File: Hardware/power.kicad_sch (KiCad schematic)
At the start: 71 parts, among them IC1 MIC5060YML-TR, J8 DeployLipo, J9 UCLipo, Q10 DMP3099L, Q11 SQS141ELNW-T1_GE3, Q12 SQS141ELNW-T1_GE3, Q5 BSZ025N04LS, Q8 DMP3099L, Q9 DMP3099L, U10 LTC4412xS6, U11 MP28167GQ-A-Z, U12 INA219AxDCN, U14 LTC4412xS6, U16 SC4215, U17 LTC4412xS6, U22 LTC4412xS6, U9 LTC4412xS6

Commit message: hardware updates
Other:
- note added: "0x45"
- note removed: "0x40"
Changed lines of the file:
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@@
 		)
 	)
-	(text "0x40"
+	(text "0x45\n"
 		(exclude_from_sim no)
 		(at 137.414 116.332 0)

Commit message: Ordering v3
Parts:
- IC1: footprint SON65P300X300X100-9N-D -> iclr:SON65P300X300X100-9N-D
- R25, R45: value 80k -> 75k
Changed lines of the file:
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@@
 			)
 		)
-		(property "Value" "80k"
+		(property "Value" "75k"
 			(at 118.11 31.7499 0)
 			(effects
@@
 			)
 		)
-		(property "Footprint" "SON65P300X300X100-9N-D"
+		(property "Footprint" "iclr:SON65P300X300X100-9N-D"
 			(at 123.19 265.1 0)
 			(effects
@@
 			)
 		)
-		(property "Value" "80k"
+		(property "Value" "75k"
 			(at 81.28 31.7499 0)
 			(effects

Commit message: Adding some 3d models
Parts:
- Q5: footprint iclr-hw:BSZ025N04LS -> iclr:BSZ025N04LS
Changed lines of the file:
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@@
 	(label "RBUS_24V_GATE"
 		(at 264.16 129.54 0)
-		(fields_autoplaced yes)
 		(effects
 			(font
@@
 	(label "Deploy_Lipo+"
 		(at 38.1 44.45 180)
-		(fields_autoplaced yes)
 		(effects
 			(font
@@
 	(label "Deploy_Lipo+"
 		(at 270.51 97.79 0)
-		(fields_autoplaced yes)
 		(effects
 			(font
@@
 	(label "BB_VCC"
 		(at 190.5 78.74 180)
-		(fields_autoplaced yes)
 		(effects
 			(font
@@
 	(label "DEP_IN"
 		(at 283.21 142.24 180)
-		(fields_autoplaced yes)
 		(effects
 			(font
@@
 	(label "BB_ALT"
 		(at 120.65 52.07 0)
-		(fields_autoplaced yes)
 		(effects
 			(font
@@
 	(label "BB_IN"
 		(at 78.74 25.4 0)
-		(fields_autoplaced yes)
 		(effects
 			(font
@@
 	(label "UC_Lipo+"
 		(at 30.48 115.57 180)
-		(fields_autoplaced yes)
 		(effects
 			(font
@@
 	(label "DEP_IN"
 		(at 95.25 120.65 90)
-		(fields_autoplaced yes)
 		(effects
 			(font
@@
 	(label "FBIn"
 		(at 247.65 31.75 180)
-		(fields_autoplaced yes)
 		(effects
 			(font
@@
 	(label "BB_SDA"
 		(at 97.79 83.82 180)
-		(fields_autoplaced yes)
 		(effects
 			(font
@@
 	(label "BB_SCL"
 		(at 97.79 78.74 180)
-		(fields_autoplaced yes)
 		(effects
 			(font
@@
 	(label "DEP_SWITCH_IN"
 		(at 95.25 129.54 270)
-		(fields_autoplaced yes)
 		(effects
 			(font
@@
 	(label "BB_OUT"
 		(at 170.18 93.98 180)
-		(fields_autoplaced yes)
 		(effects
 			(font
@@
 	(label "BB_FB"
 		(at 130.81 78.74 180)
-		(fields_autoplaced yes)
 		(effects
 			(font
@@
 	(label "DEP_IN"
 		(at 234.95 143.51 180)
-		(fields_autoplaced yes)
 		(effects
 			(font
@@
 	(label "BB_IN"
 		(at 76.2 67.31 180)
-		(fields_autoplaced yes)
 		(effects
 			(font
@@
 	(label "BB_OUT"
 		(at 223.52 71.12 180)
-		(fields_autoplaced yes)
 		(effects
 			(font
@@
 	(label "BB_VCC"
 		(at 142.24 52.07 180)
-		(fields_autoplaced yes)
 		(effects
 			(font
@@
 	(label "BB_IN"
 		(at 77.47 161.29 180)
-		(fields_autoplaced yes)
 		(effects
 			(font
@@
 	(label "BB_OUT"
 		(at 199.39 22.86 180)
-		(fields_autoplaced yes)
 		(effects
 			(font
@@
 	(label "BB_IN"
 		(at 76.2 115.57 180)
-		(fields_autoplaced yes)
 		(effects
 			(font
@@
 	(label "Deploy_Lipo+"
 		(at 245.11 100.33 180)
-		(fields_autoplaced yes)
 		(effects
 			(font
@@
 	(label "BB_FB"
 		(at 142.24 93.98 0)
-		(fields_autoplaced yes)
 		(effects
 			(font
@@
 	(label "BB_ALT"
 		(at 130.81 68.58 180)
-		(fields_autoplaced yes)
 		(effects
 			(font
@@
 	(label "BB_SDA"
 		(at 130.81 73.66 180)
-		(fields_autoplaced yes)
 		(effects
 			(font
@@
 	(label "DEP_IN"
 		(at 281.94 82.55 180)
-		(fields_autoplaced yes)
 		(effects
 			(font
@@
 	(label "DEP_IN"
 		(at 281.94 110.49 180)
-		(fields_autoplaced yes)
 		(effects
 			(font
@@
 	(label "Deploy_Lipo_Gate"
 		(at 270.51 102.87 0)
-		(fields_autoplaced yes)
 		(effects
 			(font
@@
 	(label "UC_Lipo+"
 		(at 53.34 44.45 0)
-		(fields_autoplaced yes)
 		(effects
 			(font
@@
 	(label "BB_IN"
 		(at 86.36 58.42 0)
-		(fields_autoplaced yes)
 		(effects
 			(font
@@
 	(label "BB_VCC"
 		(at 73.66 81.28 0)
-		(fields_autoplaced yes)
 		(effects
 			(font
@@
 	(label "BB_SCL"
 		(at 130.81 71.12 180)
-		(fields_autoplaced yes)
 		(effects
 			(font
@@
 	(label "Deploy_Lipo+"
 		(at 184.15 143.51 0)
-		(fields_autoplaced yes)
 		(effects
 			(font
@@
 	(label "RBUS_24V_GATE"
 		(at 270.51 74.93 0)
-		(fields_autoplaced yes)
 		(effects
 			(font
@@
 	(label "DEP_IN"
 		(at 115.57 25.4 0)
-		(fields_autoplaced yes)
 		(effects
 			(font
@@
 	(label "DEP_SWITCH_IN"
 		(at 92.71 152.4 180)
-		(fields_autoplaced yes)
 		(effects
 			(font
@@
 	(label "Deploy_Lipo_Gate"
 		(at 215.9 130.81 0)
-		(fields_autoplaced yes)
 		(effects
 			(font
@@
 		(shape input)
 		(at 91.44 172.72 180)
-		(fields_autoplaced yes)
 		(effects
 			(font
@@
 		(shape output)
 		(at 128.27 34.29 0)
-		(fields_autoplaced yes)
 		(effects
 			(font
@@
 		(shape input)
 		(at 140.97 119.38 0)
-		(fields_autoplaced yes)
 		(effects
 			(font
@@
 		(shape input)
 		(at 30.48 67.31 180)
-		(fields_autoplaced yes)
 		(effects
 			(font
@@
 		(shape input)
 		(at 250.19 142.24 180)
-		(fields_autoplaced yes)
 		(effects
 			(font
@@
 		(shape input)
 		(at 240.03 72.39 180)
-		(fields_autoplaced yes)
 		(effects
 			(font
@@
 		(shape output)
 		(at 175.26 118.11 0)
-		(fields_autoplaced yes)
 		(effects
 			(font
@@
 		(shape input)
 		(at 270.51 69.85 0)
-		(fields_autoplaced yes)
 		(effects
 			(font
@@
 		(shape input)
 		(at 140.97 121.92 0)
-		(fields_autoplaced yes)
 		(effects
 			(font
@@
 		(shape output)
 		(at 91.44 34.29 0)
-		(fields_autoplaced yes)
 		(effects
 			(font
@@
 			)
 		)
-		(property "Footprint" "iclr-hw:BSZ025N04LS"
+		(property "Footprint" "iclr:BSZ025N04LS"
 			(at 206.68 132.08 0)
 			(effects

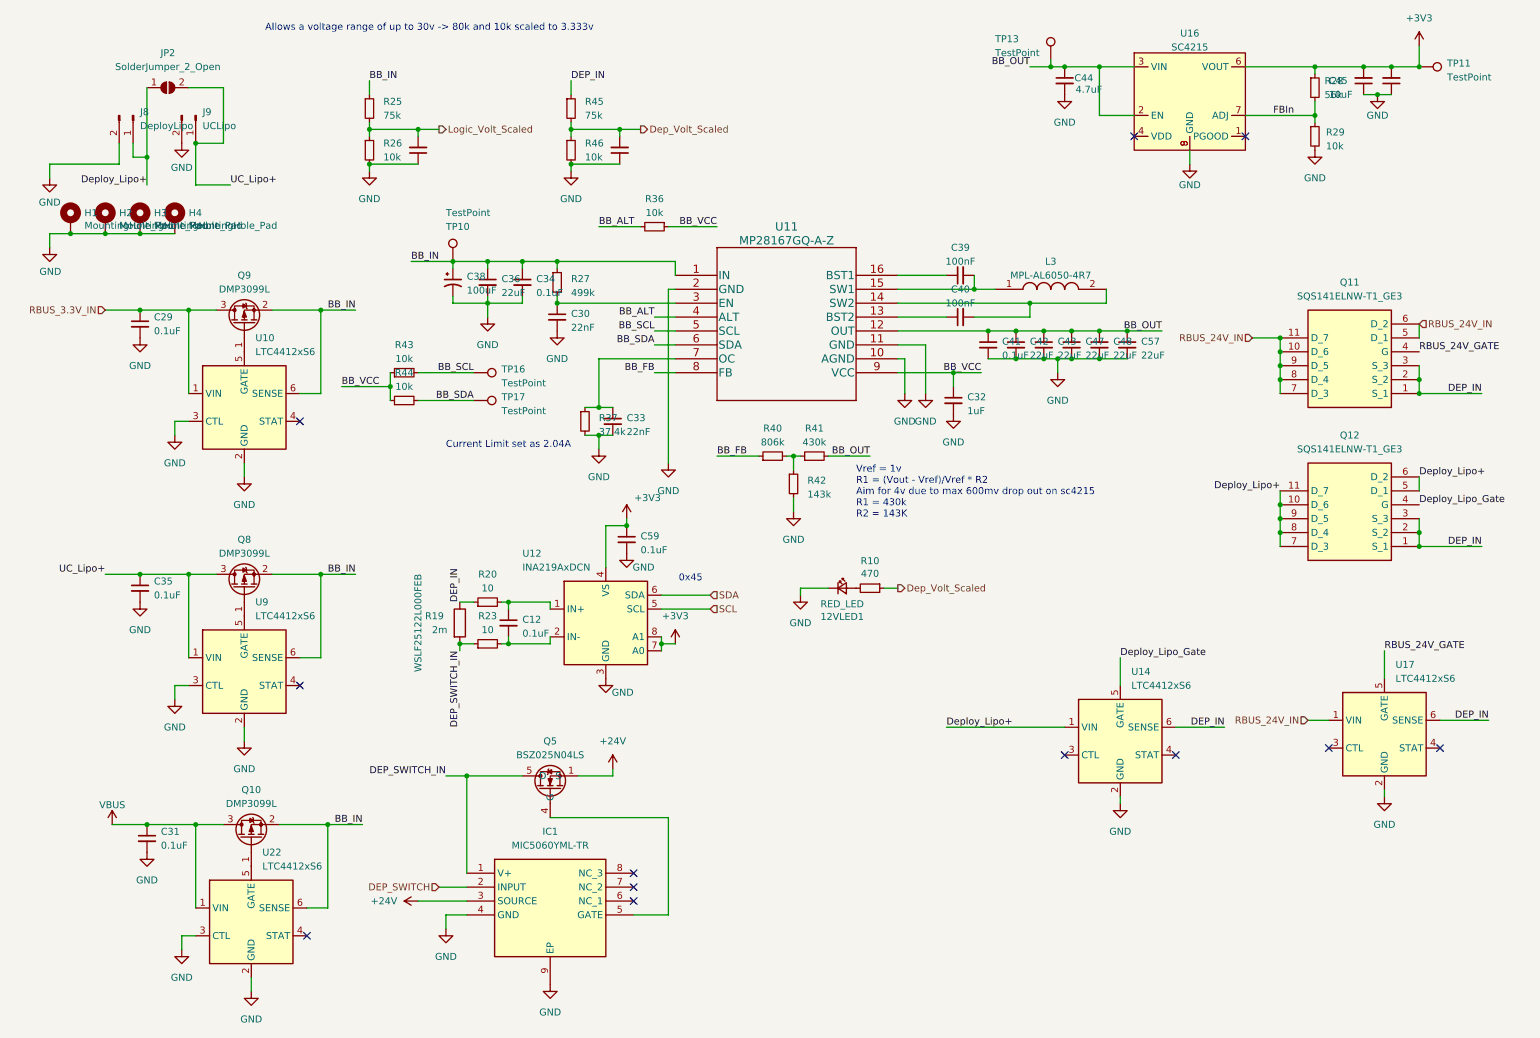
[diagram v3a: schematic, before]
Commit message: cleaned up schematic and bom
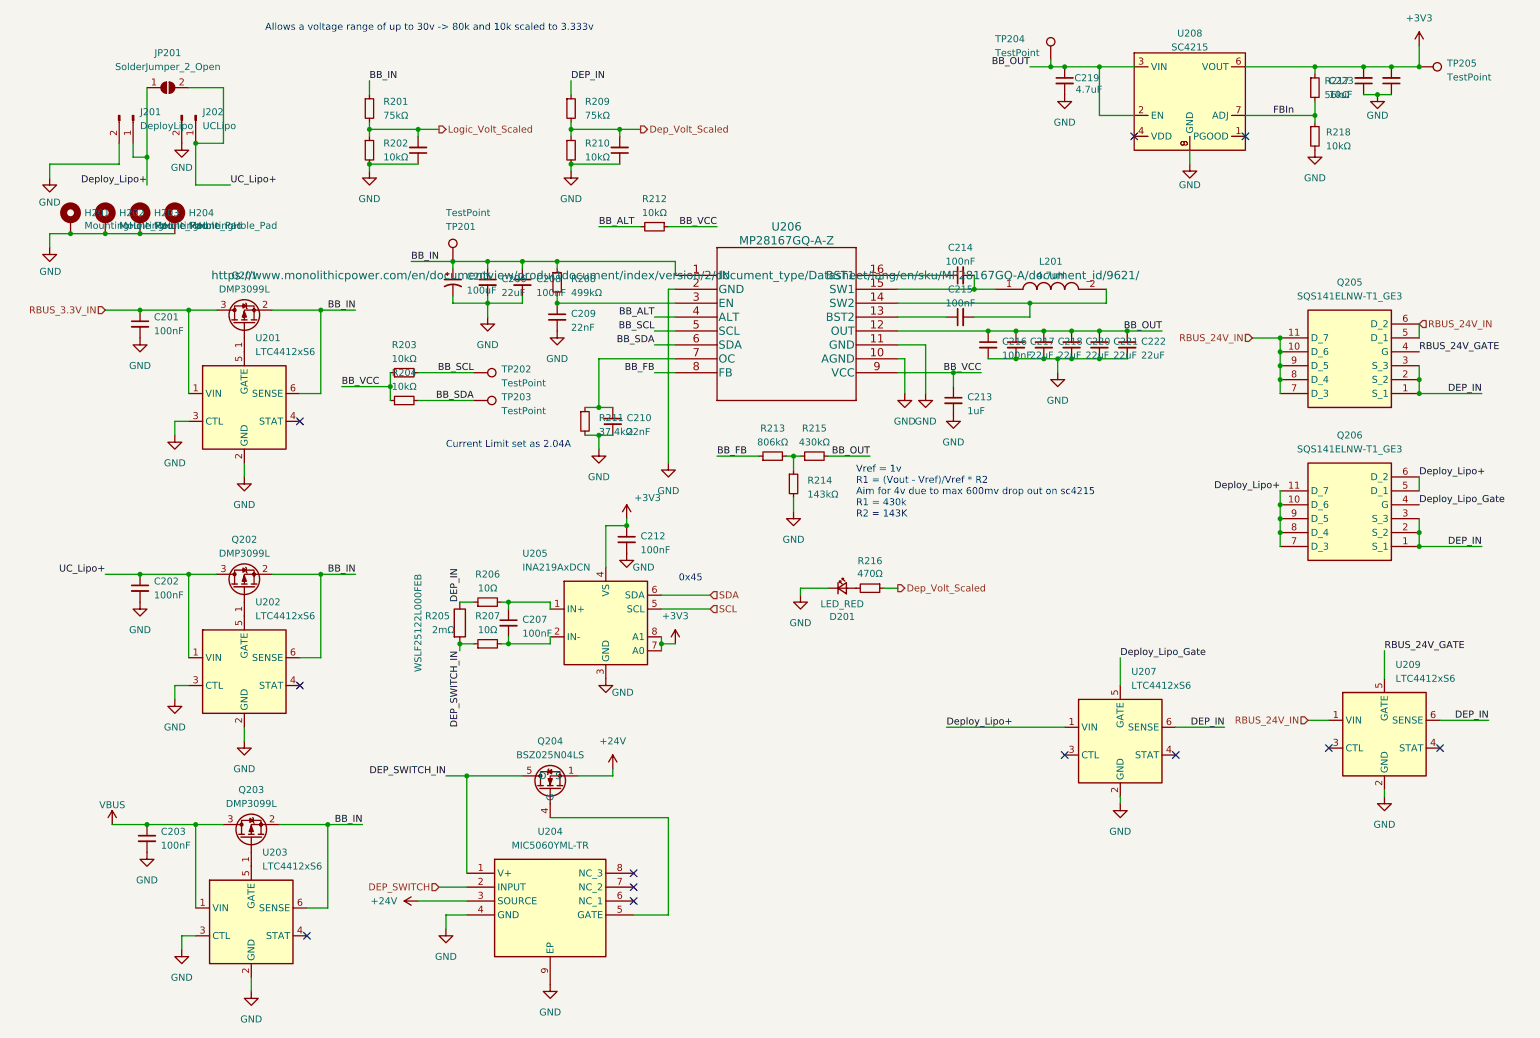
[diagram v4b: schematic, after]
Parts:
- C201: renamed from C29; value 0.1uF -> 100nF
- C202: renamed from C35; value 0.1uF -> 100nF
- C203: renamed from C31; value 0.1uF -> 100nF
- C204: renamed from C37; value 0.1uF -> 100nF
- C207: renamed from C12; value 0.1uF -> 100nF
- C208: renamed from C34; value 0.1uF -> 100nF
- C211: renamed from C58; value 0.1uF -> 100nF
- C212: renamed from C59; value 0.1uF -> 100nF
- C216: renamed from C41; value 0.1uF -> 100nF
- C224: renamed from C46; value 0.1uF -> 100nF
- D201: renamed from 12VLED1; value RED_LED -> LED_RED
- H201: renamed from H1; now left out of the parts list
- H202: renamed from H2; now left out of the parts list
- H203: renamed from H3; now left out of the parts list
- H204: renamed from H4; now left out of the parts list
- JP201: renamed from JP2; now left out of the parts list
- L201: renamed from L3; value MPL-AL6050-4R7 -> 4.7uH
- R201: renamed from R25; value 75k -> 75kΩ
- R202: renamed from R26; value 10k -> 10kΩ
- R203: renamed from R43; value 10k -> 10kΩ
- R204: renamed from R44; value 10k -> 10kΩ
- R205: renamed from R19; value 2m -> 2mΩ
- R206: renamed from R20; value 10 -> 10Ω
- R207: renamed from R23; value 10 -> 10Ω
- R208: renamed from R27; value 499k -> 499kΩ
- R209: renamed from R45; value 75k -> 75kΩ
- R210: renamed from R46; value 10k -> 10kΩ
- R211: renamed from R37; value 37.4k -> 37.4kΩ
- R212: renamed from R36; value 10k -> 10kΩ
- R213: renamed from R40; value 806k -> 806kΩ
- R214: renamed from R42; value 143k -> 143kΩ
- R215: renamed from R41; value 430k -> 430kΩ
- R216: renamed from R10; value 470 -> 470Ω
- R217: renamed from R28; value 56k -> 56kΩ
- R218: renamed from R29; value 10k -> 10kΩ
- TP201: renamed from TP10; now left out of the parts list
- TP202: renamed from TP16; now left out of the parts list
- TP203: renamed from TP17; now left out of the parts list
- TP204: renamed from TP13; now left out of the parts list
- TP205: renamed from TP11; now left out of the parts list
- renumbered C38 to C205, C36 to C206, C30 to C209, C33 to C210, C32 to C213, C39 to C214, C40 to C215, C42 to C217, C43 to C218, C44 to C219, C47 to C220, C48 to C221, C57 to C222, C45 to C223, J8 to J201, J9 to J202, Q9 to Q201, Q8 to Q202, Q10 to Q203, Q5 to Q204, Q11 to Q205, Q12 to Q206, U10 to U201, U9 to U202, U22 to U203, IC1 to U204, U12 to U205, U11 to U206, U14 to U207, U16 to U208, U17 to U209

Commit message: updated resistors w cap footprints
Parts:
- R203, R204, R208, R211, R212, R213, R214, R215: footprint Capacitor_SMD:C_0402_1005Metric -> Resistor_SMD:R_0402_1005Metric
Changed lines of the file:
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@@
 			)
 		)
-		(property "Footprint" "Capacitor_SMD:C_0402_1005Metric"
+		(property "Footprint" "Resistor_SMD:R_0402_1005Metric"
 			(at 85.09 83.82 0)
 			(effects
@@
 			)
 		)
-		(property "Footprint" "Capacitor_SMD:C_0402_1005Metric"
+		(property "Footprint" "Resistor_SMD:R_0402_1005Metric"
 			(at 118.11 87.63 0)
 			(effects
@@
 			)
 		)
-		(property "Footprint" "Capacitor_SMD:C_0402_1005Metric"
+		(property "Footprint" "Resistor_SMD:R_0402_1005Metric"
 			(at 113.03 62.23 0)
 			(effects
@@
 			)
 		)
-		(property "Footprint" "Capacitor_SMD:C_0402_1005Metric"
+		(property "Footprint" "Resistor_SMD:R_0402_1005Metric"
 			(at 130.81 52.07 0)
 			(effects
@@
 			)
 		)
-		(property "Footprint" "Capacitor_SMD:C_0402_1005Metric"
+		(property "Footprint" "Resistor_SMD:R_0402_1005Metric"
 			(at 156.21 99.06 0)
 			(effects
@@
 			)
 		)
-		(property "Footprint" "Capacitor_SMD:C_0402_1005Metric"
+		(property "Footprint" "Resistor_SMD:R_0402_1005Metric"
 			(at 152.4 93.98 0)
 			(effects
@@
 			)
 		)
-		(property "Footprint" "Capacitor_SMD:C_0402_1005Metric"
+		(property "Footprint" "Resistor_SMD:R_0402_1005Metric"
 			(at 160.02 93.98 0)
 			(effects
@@
 			)
 		)
-		(property "Footprint" "Capacitor_SMD:C_0402_1005Metric"
+		(property "Footprint" "Resistor_SMD:R_0402_1005Metric"
 			(at 85.09 78.74 0)
 			(effects

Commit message: continued
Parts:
- Q205, Q206: footprint iclr-hw:SQS850ENT1_GE3 -> iclr:SQS850ENT1_GE3
- U208: value SC4215 -> SC4215ASTRT
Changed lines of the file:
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@@
 		(fields_autoplaced yes)
 		(property "Reference" "U208"
-			(at 228.6 16.7472 0)
-			(effects
-				(font
-					(size 1.27 1.27)
-				)
-			)
-		)
-		(property "Value" "SC4215"
-			(at 228.6 19.2841 0)
+			(at 228.6 15.24 0)
+			(effects
+				(font
+					(size 1.27 1.27)
+				)
+			)
+		)
+		(property "Value" "SC4215ASTRT"
+			(at 228.6 17.78 0)
 			(effects
 				(font
@@
 			)
 		)
-		(property "Footprint" "iclr-hw:SQS850ENT1_GE3"
+		(property "Footprint" "iclr:SQS850ENT1_GE3"
 			(at 248.92 15.57 0)
 			(effects
@@
 			)
 		)
-		(property "Footprint" "iclr-hw:SQS850ENT1_GE3"
+		(property "Footprint" "iclr:SQS850ENT1_GE3"
 			(at 248.92 -12.37 0)
 			(effects
